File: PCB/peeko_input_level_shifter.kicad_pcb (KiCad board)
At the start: 2 copper layers, 27.9 x 43.2 mm, 21 parts, among them J1 Conn_02x15_Odd_Even, J2 Conn_02x15_Odd_Even, U1 TXU0104, U2 TXU0104, U3 TXU0104, U4 TXU0104, U5 TXU0104, U6 TXU0104

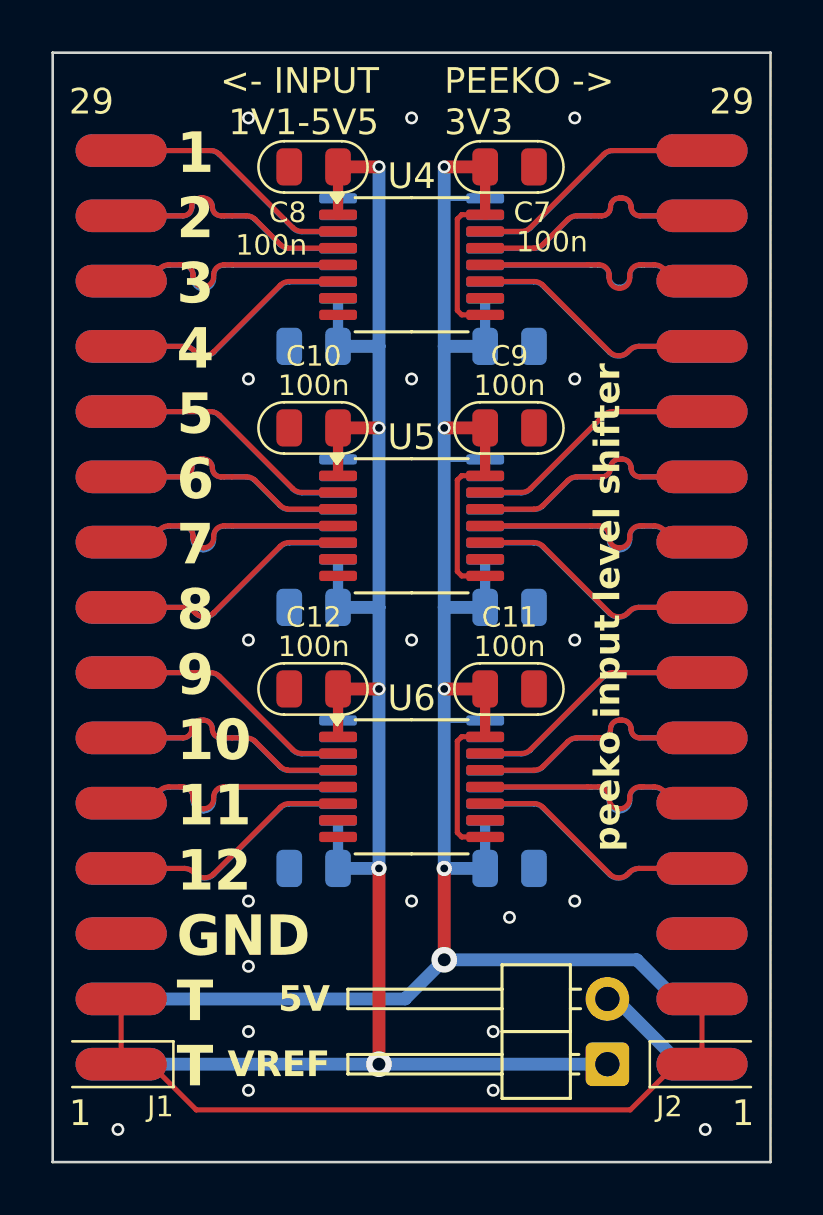
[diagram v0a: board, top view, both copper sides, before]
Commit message: shrink level shifter
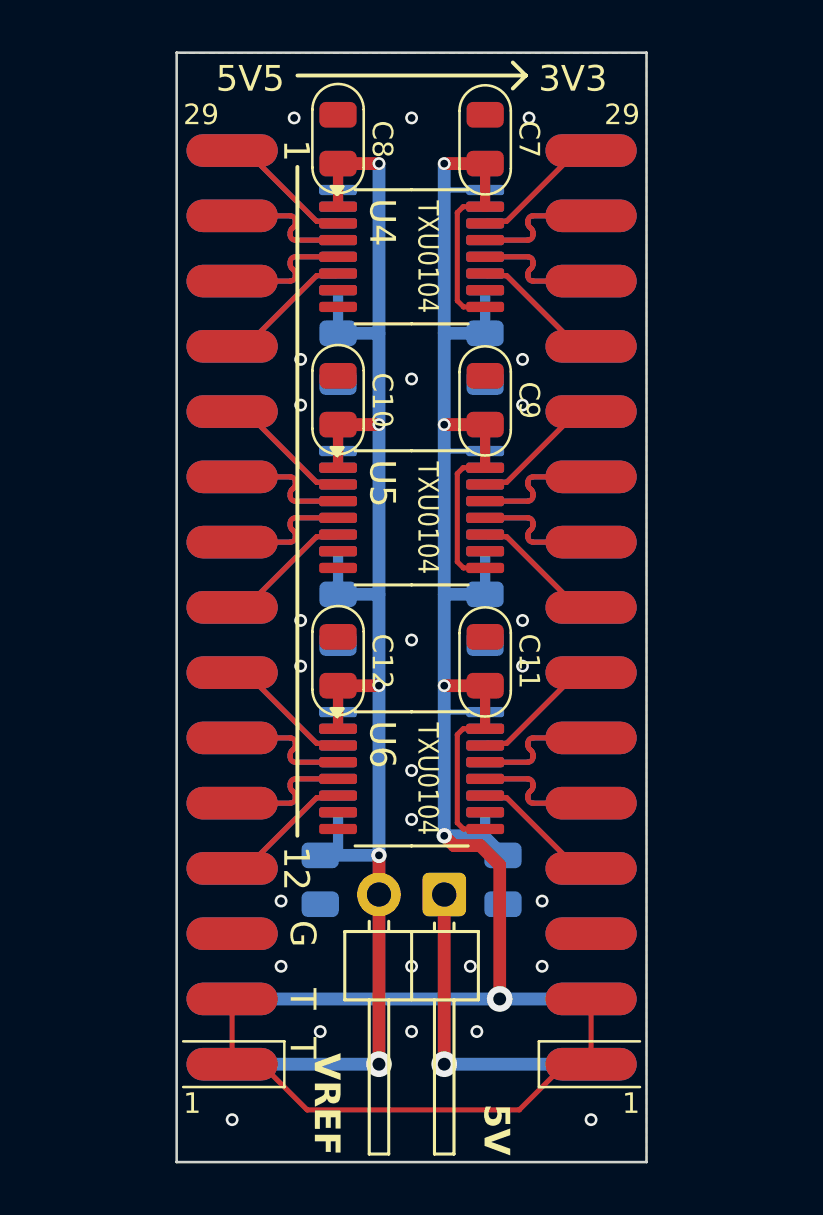
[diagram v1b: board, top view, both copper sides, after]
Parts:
- moved JP1 9.16 mm to (161.2, 107.2), turned to -90 degrees
- moved J1 4.32 mm to (150.8, 96.0)
- moved J2 4.32 mm to (169.0, 96.0)
- moved C10 1.44 mm to (157.0, 88.0), turned to -90 degrees
- moved C12 1.44 mm to (157.0, 98.1), turned to -90 degrees
- moved C8 1.44 mm to (157.0, 77.8), turned to -90 degrees
- moved C11 1.44 mm to (162.8, 98.1), turned to 90 degrees
- moved C7 1.44 mm to (162.8, 77.8), turned to 90 degrees
- moved C9 1.44 mm to (162.8, 88.0), turned to 90 degrees
- moved C5 1.05 mm to (162.8, 86.3), turned to -90 degrees
- moved C3 1.05 mm to (162.8, 96.5), turned to -90 degrees
- moved C6 1.05 mm to (157.0, 86.3), turned to 90 degrees
- moved C4 1.05 mm to (157.0, 96.5), turned to 90 degrees
- moved C1 0.51 mm to (163.5, 106.6), turned to -90 degrees
- moved C2 0.51 mm to (156.3, 106.6), turned to 90 degrees
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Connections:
- JP1 pad 1: VREF -> +5V
- JP1 pad 2: +5V -> VREF
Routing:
- net VREF: track 74.6 -> 60.4 mm
- net /EXT_T: track 29.2 -> 20.5 mm
- net +5V: track 4.74 -> 12.3 mm, vias 0 -> 1
- net +3V3: track 97.8 -> 91.0 mm
- net /CHAN_2_OUT: track 9.76 -> 5.14 mm
- net /CHAN_17_OUT: track 9.76 -> 5.14 mm
- net /CHAN_13_OUT: track 9.76 -> 5.14 mm
- net /CHAN_17_IN: track 9.76 -> 5.14 mm
- net /CHAN_13_IN: track 9.76 -> 5.14 mm
- net /CHAN_21_IN: track 9.76 -> 5.14 mm
- net /CHAN_9_IN: track 9.65 -> 5.14 mm
- net /CHAN_22_IN: track 9.65 -> 5.14 mm
- net /CHAN_14_IN: track 9.65 -> 5.14 mm
- net /CHAN_18_IN: track 9.65 -> 5.14 mm
- net /CHAN_14_OUT: track 9.65 -> 5.14 mm
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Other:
- board size 27.9 x 43.2 mm -> 18.3 x 43.2 mm
- board text added: "12"
- board text added: "13"
- board text added: "24"
- board text added: "3V3"
- board text added: "5V5"
- board text added: "G"
- board text added: "GND"
- board text added: "T"
- board text removed: "1 2 3 4 5 6 7 8 9 10 11 12 GND T T"
- board text removed: "24 23 22 21 20 19 18 17 16 15 14 13 GND 3V3 VREF"
- board text removed: "<- INPUT 1V1-5V5"
- board text removed: "PEEKO -> 3V3"
- board text removed: "to peeko"

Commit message: renumber level shifter
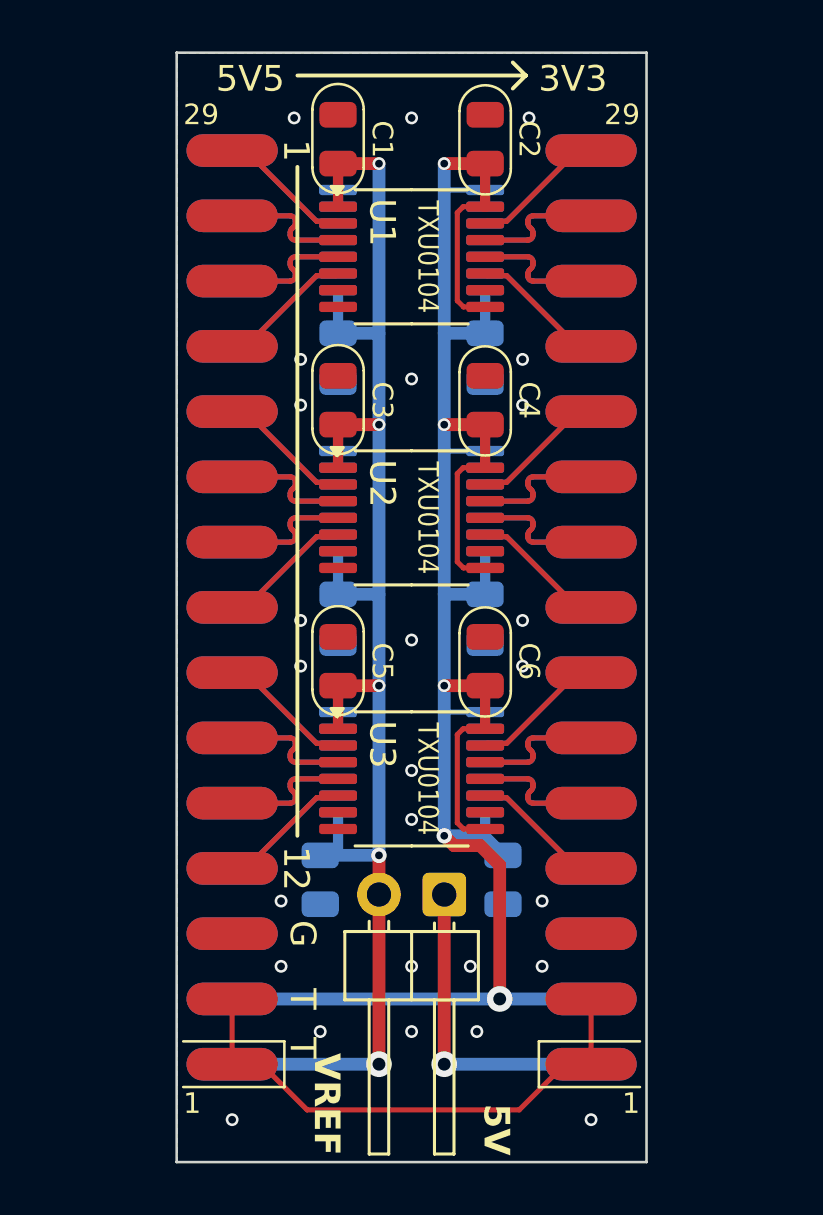
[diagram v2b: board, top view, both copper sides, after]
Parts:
- renumbered C8 to C1, C3 to C10, C6 to C11, C5 to C12, C7 to C2, C10 to C3, C9 to C4, C12 to C5, C11 to C6, C2 to C7, C1 to C8, C4 to C9, U4 to U1, U5 to U2, U6 to U3, U1 to U4, U2 to U5, U3 to U6
